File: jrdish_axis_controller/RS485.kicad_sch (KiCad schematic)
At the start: 38 parts, among them CN10 KF2EDGR-2.54-4P, CN11 KF2EDGR-2.54-4P, CN9 KF2EDGR-2.54-4P, U2 ISOW1432BDFMR, U3 ISOW1432BDFMR

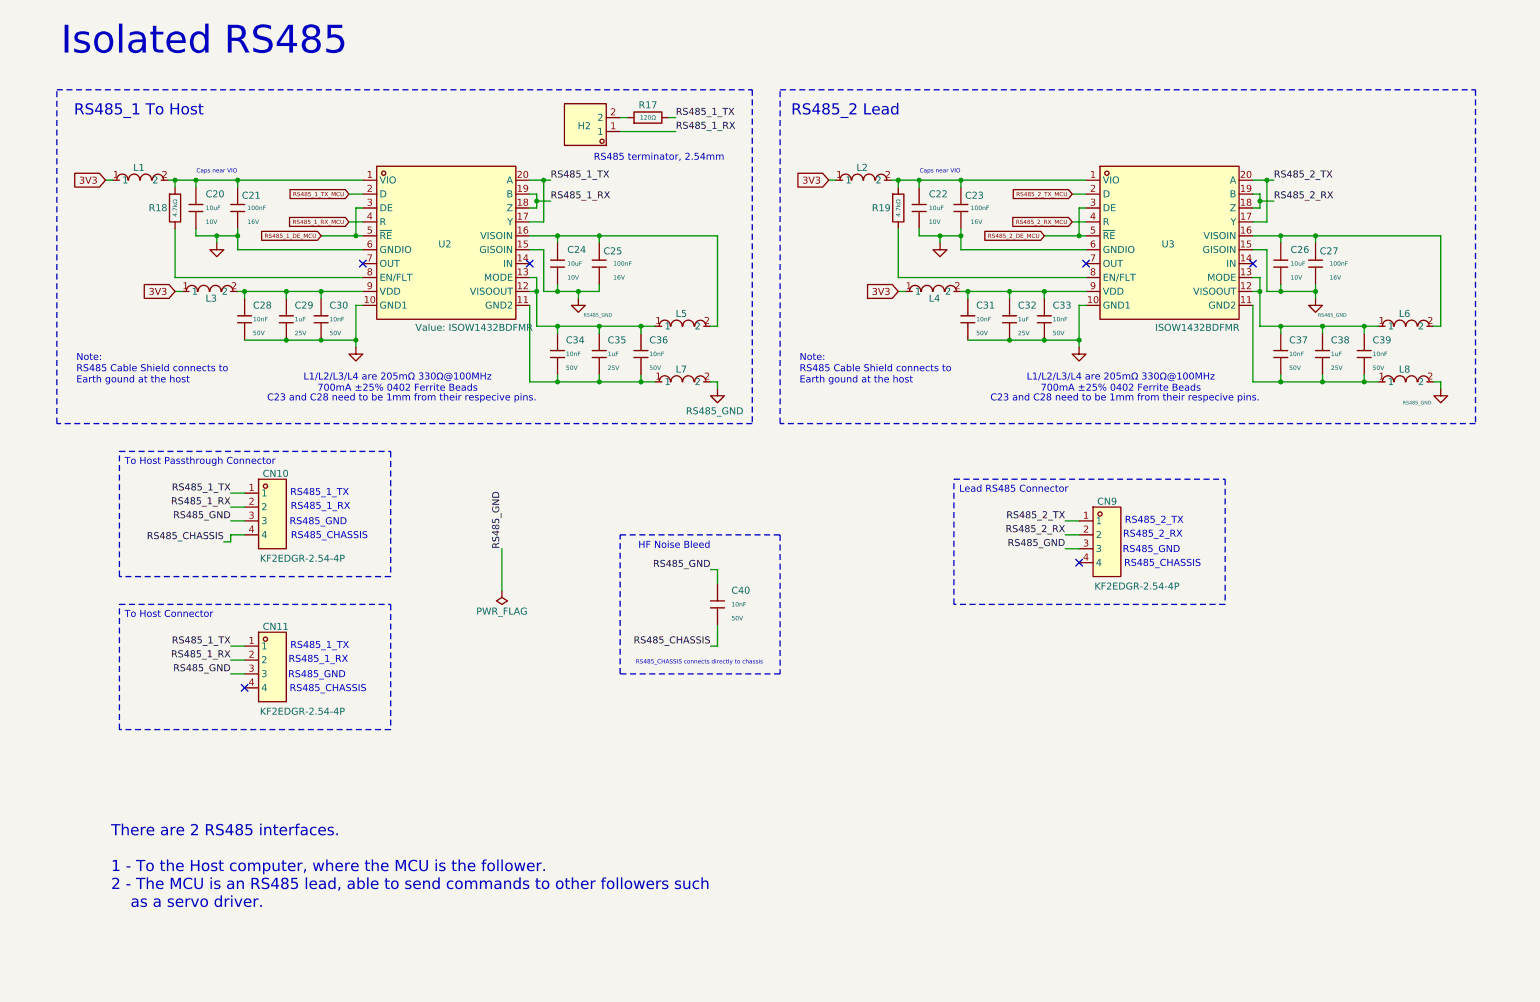
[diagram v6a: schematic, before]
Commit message: RS485 isolated areas in place
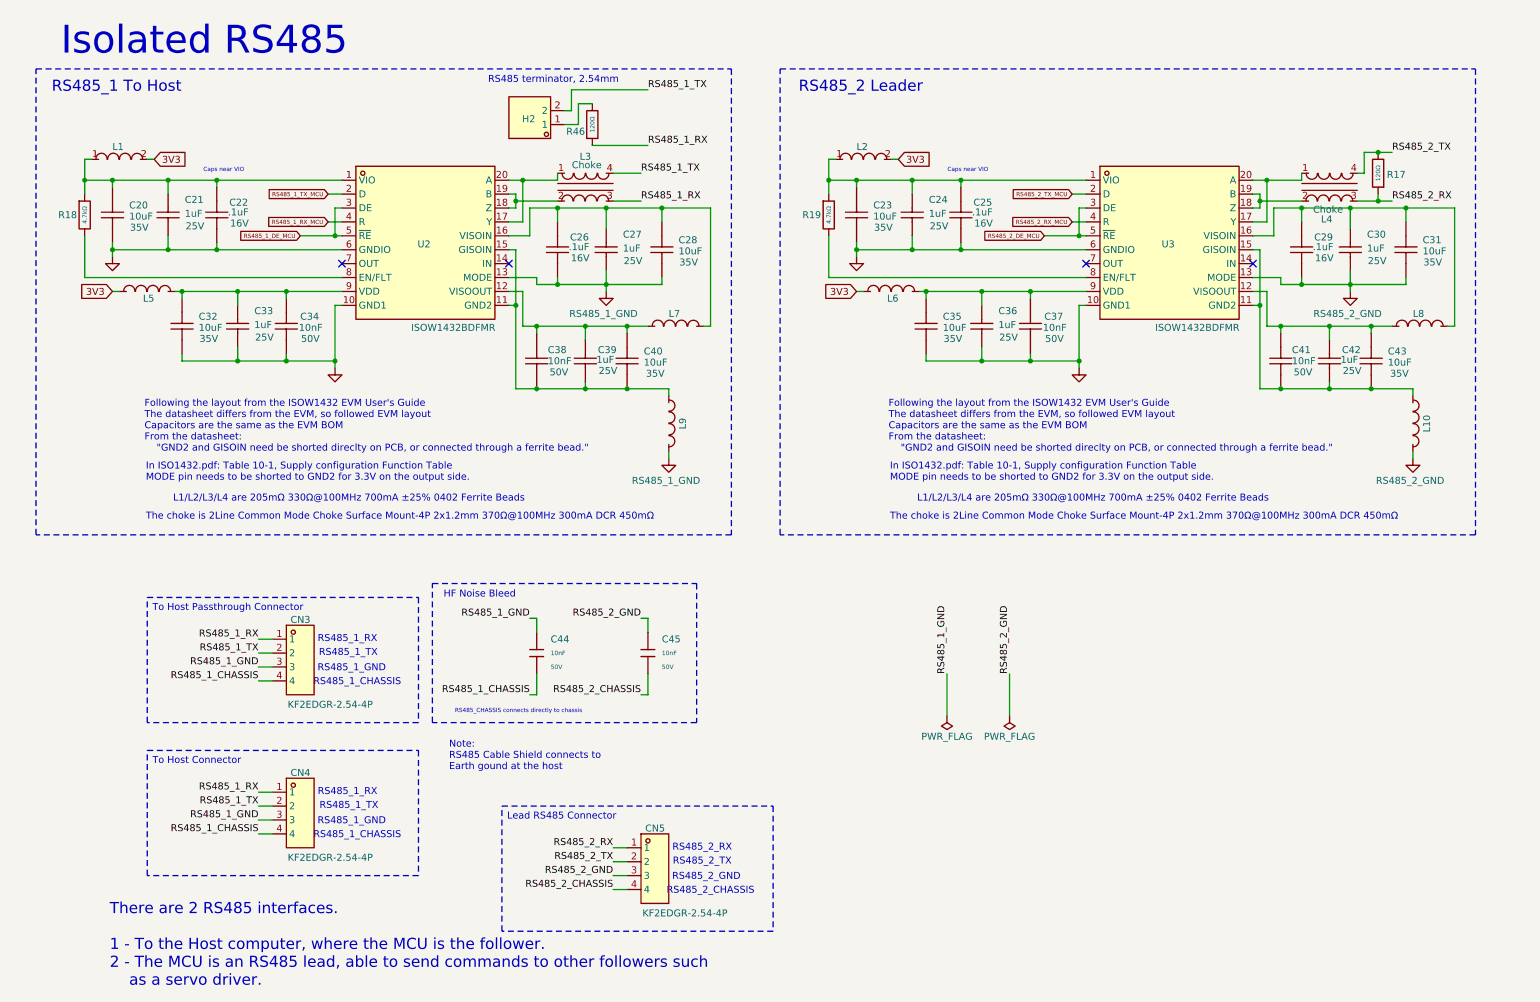
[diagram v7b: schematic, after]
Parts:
- removed C20, C22, C24, C26: 10uF, PCM_JLCPCB:C_0603, symbol PCM_JLCPCB-Capacitors:0603,10uF
- removed C21, C23, C25, C27: 100nF, PCM_JLCPCB:C_0402, symbol PCM_JLCPCB-Capacitors:0402,100nF
- removed C28, C30, C31, C33, C34, C36, C37, C39: 10nF, PCM_JLCPCB:C_0402, symbol PCM_JLCPCB-Capacitors:0402,10nF
- removed C29, C32, C35, C38: 1uF, PCM_JLCPCB:C_0402, symbol PCM_JLCPCB-Capacitors:0402,1uF
- removed L4: BLM15EX331SN1D, MyParts:L0402, symbol MyParts:BLM15EX331SN1D
- added C20, C23, C28, C31, C32, C35, C40, C43: 10uF, MyParts:C0805, symbol MyParts:GRM21BR6YA106KE43L
- added C21, C24, C27, C30, C33, C36, C39, C42: 1uF, MyParts:C0603, symbol MyParts:CL10A105KA8NNNC
- added C22, C25, C26, C29: .1uF, MyParts:C0402, symbol MyParts:CL05B104KO5NNNC
- added C34, C37, C38, C41: 10nF, MyParts:C0402, symbol MyParts:0402B103K500CT
- added C45: 10nF, PCM_JLCPCB:C_0402, symbol PCM_JLCPCB-Capacitors:0402,10nF
- added L10: BLM15EX331SN1D, MyParts:L0402, symbol MyParts:BLM15EX331SN1D
- added L3, L4: Choke, MyParts:FILTER-SMD_4P-L2.0-W1.2-BL, symbol MyParts:SMW2012B371BTE
- added R46: 120Ω, PCM_JLCPCB:R_0805, symbol PCM_JLCPCB-Resistors:0805,120Ω
- renumbered C40 to C44, CN10 to CN3, CN11 to CN4, CN9 to CN5, L3 to L5, L5 to L7, L7 to L9
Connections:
- net RS485_CHASSIS is gone; now on net RS485_1_CHASSIS: C44.2, CN3.4
- net 3V3: now also L1.2, L2.2, L6.1; no longer L1.1, L2.1
- net GND: now also C20.1, C21.2, C22.2, C23.1, C24.2, C25.2, C32.1, C33.2, C34.2, C35.1, C36.2, C37.2
- net RS485_1_RX: now also CN3.1, CN4.1, L3.3, R46.1; no longer CN3.2, CN4.2, H2.1, U2.18 (Z), U2.19 (B)
- net RS485_1_TX: now also CN3.2, CN4.2, H2.2, L3.4; no longer CN3.1, CN4.1, R17.2, U2.17 (Y), U2.20 (A)
- net RS485_2_RX: now also CN5.1, R17.1, L4.3; no longer CN5.2, U3.18 (Z), U3.19 (B)
- net RS485_2_TX: now also CN5.2, R17.2, L4.4; no longer CN5.1, U3.17 (Y), U3.20 (A)
- net at L5.2, U2.9 (VDD): now also C32.2, C33.1, C34.1
- net at U3.16 (VISOIN): now also L8.2, C29.1, C30.1, C31.2; no longer L6.2
- net at R19.1, U3.1 (VIO): now also L2.1, C23.2, C24.1, C25.1; no longer L2.2
- net at L7.1, U2.12 (VISOOUT): now also C38.1, C39.1, C40.2; no longer U2.13 (MODE)
- net at L9.1, U2.11 (GND2): now also U2.15 (GISOIN), C38.2, C39.2, C40.1
- net at L7.2, U2.16 (VISOIN): now also C26.1, C27.1, C28.2
- net at R18.1, U2.1 (VIO): now also L1.1, C20.2, C21.1, C22.1; no longer L1.2
- net at U3.9 (VDD): now also L6.2, C35.2, C36.1, C37.1
- net at L8.1: now also U3.12 (VISOOUT), C41.1, C42.1, C43.2; no longer U3.11 (GND2)
- net RS485_1_CHASSIS: now reaches CN4.4
- net RS485_2_CHASSIS: now reaches CN5.4
- net RS485_2_CHASSIS: now also C45.2
- net RS485_GND renamed RS485_1_GND
- net RS485_1_GND: now also U2.13 (MODE), C26.2, C27.2, C28.1; no longer CN5.3, L8.2, U2.15 (GISOIN), U3.15 (GISOIN)
- new net: C41.2, C42.2, C43.1, L10.1, U3.11 (GND2), U3.15 (GISOIN)
- new net: H2.1, R46.2
- new net: L4.1, U3.17 (Y), U3.20 (A)
- new net: L4.2, U3.18 (Z), U3.19 (B)
- new net: L3.1, U2.17 (Y), U2.20 (A)
- new net: L3.2, U2.18 (Z), U2.19 (B)
- new net RS485_2_GND: C29.2, C30.2, C31.1, C45.1, CN5.3, L10.2, U3.13 (MODE)
- no-connect marks 6 -> 4
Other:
- note added: "Following the layout from the ISOW1432 EVM User's Guide The datasheet differs from the EVM, so followed EVM layout Capacitors are the same as the EVM BOM From the datasheet: "GND2 and GISOIN need be shorted direclty on PCB, or connected through a ferrite bead.""
- note added: "In ISO1432.pdf: Table 10-1, Supply configuration Function Table MODE pin needs to be shorted to GND2 for 3.3V on the output side."
- note added: "RS485_1_CHASSIS"
- note added: "RS485_1_GND"
- note added: "RS485_2 Leader"
- note added: "RS485_2_CHASSIS"
- note added: "RS485_2_GND"
- note added: "The choke is 2Line Common Mode Choke Surface Mount-4P 2x1.2mm 370Ω@100MHz 300mA DCR 450mΩ"
- note removed: "C23 and C28 need to be 1mm from their respecive pins."
- note removed: "RS485_2 Lead"
- note removed: "RS485_CHASSIS"
- note removed: "RS485_GND"
- moved on the sheet: C44, CN3, CN4, CN5, H2, R18, U2

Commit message: Layout complete
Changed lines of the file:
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@@
 	)
 	(symbol
+		(lib_name "CL10A105KA8NNNC_7")
 		(lib_id "MyParts:CL10A105KA8NNNC")
 		(at 255.27 58.42 270)
@@
 			)
 		)
-		(property "Datasheet" "https://www.lcsc.com/datasheet/C5673.pdf?spm=wm.sxq.inf.ggs___wm.ssy.bg.0.cbh&lcsc_vid=FFBaV1wHQFldUVICFgBfBVJTQVJWXgBfEQRYBAFQE1YxVlNRQFNXUV1UR1laVDsOAxUeFF5JWBYZEEoKFBINSQcJGk4dAgUUFAk%3D"
+		(property "Datasheet" "https://lcsc.com/product-detail/Multilayer-Ceramic-Capacitors-MLCC-SMD-SMT_SAMSUNG_CL10A105KA8NNNC_1uF-105-10-25V_C5673.html"
 			(at 245.11 58.42 0)
 			(hide yes)
@@
 	)
 	(symbol
+		(lib_name "CL10A105KA8NNNC_5")
 		(lib_id "MyParts:CL10A105KA8NNNC")
 		(at 175.26 52.07 270)
@@
 			)
 		)
-		(property "Datasheet" "https://www.lcsc.com/datasheet/C5673.pdf?spm=wm.sxq.inf.ggs___wm.ssy.bg.0.cbh&lcsc_vid=FFBaV1wHQFldUVICFgBfBVJTQVJWXgBfEQRYBAFQE1YxVlNRQFNXUV1UR1laVDsOAxUeFF5JWBYZEEoKFBINSQcJGk4dAgUUFAk%3D"
+		(property "Datasheet" "https://lcsc.com/product-detail/Multilayer-Ceramic-Capacitors-MLCC-SMD-SMT_SAMSUNG_CL10A105KA8NNNC_1uF-105-10-25V_C5673.html"
 			(at 165.1 52.07 0)
 			(hide yes)
@@
 	)
 	(symbol
+		(lib_name "CL10A105KA8NNNC_3")
 		(lib_id "MyParts:CL10A105KA8NNNC")
 		(at 39.37 52.07 270)
@@
 			)
 		)
-		(property "Datasheet" "https://www.lcsc.com/datasheet/C5673.pdf?spm=wm.sxq.inf.ggs___wm.ssy.bg.0.cbh&lcsc_vid=FFBaV1wHQFldUVICFgBfBVJTQVJWXgBfEQRYBAFQE1YxVlNRQFNXUV1UR1laVDsOAxUeFF5JWBYZEEoKFBINSQcJGk4dAgUUFAk%3D"
+		(property "Datasheet" "https://lcsc.com/product-detail/Multilayer-Ceramic-Capacitors-MLCC-SMD-SMT_SAMSUNG_CL10A105KA8NNNC_1uF-105-10-25V_C5673.html"
 			(at 29.21 52.07 0)
 			(hide yes)
@@
 	)
 	(symbol
+		(lib_name "CL10A105KA8NNNC_2")
 		(lib_id "MyParts:CL10A105KA8NNNC")
 		(at 115.57 78.74 270)
@@
 			)
 		)
-		(property "Datasheet" "https://www.lcsc.com/datasheet/C5673.pdf?spm=wm.sxq.inf.ggs___wm.ssy.bg.0.cbh&lcsc_vid=FFBaV1wHQFldUVICFgBfBVJTQVJWXgBfEQRYBAFQE1YxVlNRQFNXUV1UR1laVDsOAxUeFF5JWBYZEEoKFBINSQcJGk4dAgUUFAk%3D"
+		(property "Datasheet" "https://lcsc.com/product-detail/Multilayer-Ceramic-Capacitors-MLCC-SMD-SMT_SAMSUNG_CL10A105KA8NNNC_1uF-105-10-25V_C5673.html"
 			(at 105.41 78.74 0)
 			(hide yes)
@@
 	)
 	(symbol
+		(lib_name "CL10A105KA8NNNC_1")
 		(lib_id "MyParts:CL10A105KA8NNNC")
 		(at 119.38 58.42 270)
@@
 			)
 		)
-		(property "Datasheet" "https://www.lcsc.com/datasheet/C5673.pdf?spm=wm.sxq.inf.ggs___wm.ssy.bg.0.cbh&lcsc_vid=FFBaV1wHQFldUVICFgBfBVJTQVJWXgBfEQRYBAFQE1YxVlNRQFNXUV1UR1laVDsOAxUeFF5JWBYZEEoKFBINSQcJGk4dAgUUFAk%3D"
+		(property "Datasheet" "https://lcsc.com/product-detail/Multilayer-Ceramic-Capacitors-MLCC-SMD-SMT_SAMSUNG_CL10A105KA8NNNC_1uF-105-10-25V_C5673.html"
 			(at 109.22 58.42 0)
 			(hide yes)
@@
 	)
 	(symbol
+		(lib_name "CL10A105KA8NNNC_4")
 		(lib_id "MyParts:CL10A105KA8NNNC")
 		(at 52.07 72.39 270)
@@
 			)
 		)
-		(property "Datasheet" "https://www.lcsc.com/datasheet/C5673.pdf?spm=wm.sxq.inf.ggs___wm.ssy.bg.0.cbh&lcsc_vid=FFBaV1wHQFldUVICFgBfBVJTQVJWXgBfEQRYBAFQE1YxVlNRQFNXUV1UR1laVDsOAxUeFF5JWBYZEEoKFBINSQcJGk4dAgUUFAk%3D"
+		(property "Datasheet" "https://lcsc.com/product-detail/Multilayer-Ceramic-Capacitors-MLCC-SMD-SMT_SAMSUNG_CL10A105KA8NNNC_1uF-105-10-25V_C5673.html"
 			(at 41.91 72.39 0)
 			(hide yes)
@@
 	)
 	(symbol
+		(lib_name "CL10A105KA8NNNC_6")
 		(lib_id "MyParts:CL10A105KA8NNNC")
 		(at 187.96 72.39 270)
@@
 			)
 		)
-		(property "Datasheet" "https://www.lcsc.com/datasheet/C5673.pdf?spm=wm.sxq.inf.ggs___wm.ssy.bg.0.cbh&lcsc_vid=FFBaV1wHQFldUVICFgBfBVJTQVJWXgBfEQRYBAFQE1YxVlNRQFNXUV1UR1laVDsOAxUeFF5JWBYZEEoKFBINSQcJGk4dAgUUFAk%3D"
+		(property "Datasheet" "https://lcsc.com/product-detail/Multilayer-Ceramic-Capacitors-MLCC-SMD-SMT_SAMSUNG_CL10A105KA8NNNC_1uF-105-10-25V_C5673.html"
 			(at 177.8 72.39 0)
 			(hide yes)
@@
 			)
 		)
-		(property "Datasheet" "https://www.lcsc.com/datasheet/C5673.pdf?spm=wm.sxq.inf.ggs___wm.ssy.bg.0.cbh&lcsc_vid=FFBaV1wHQFldUVICFgBfBVJTQVJWXgBfEQRYBAFQE1YxVlNRQFNXUV1UR1laVDsOAxUeFF5JWBYZEEoKFBINSQcJGk4dAgUUFAk%3D"
+		(property "Datasheet" "https://lcsc.com/product-detail/Multilayer-Ceramic-Capacitors-MLCC-SMD-SMT_SAMSUNG_CL10A105KA8NNNC_1uF-105-10-25V_C5673.html"
 			(at 241.3 78.74 0)
 			(hide yes)
